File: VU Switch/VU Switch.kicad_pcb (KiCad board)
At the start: 2 copper layers, 99.1 x 59.7 mm, 2 parts

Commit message: Blank PCB
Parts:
- added M1: Mounting_pin, Mounting:M3, F.Cu at (104.8, 106.0)
- added M2: Mounting_pin, Mounting:M3, F.Cu at (197.5, 106.0)
- added M3: Mounting_pin, Mounting:M3, F.Cu at (197.5, 52.7)
- added M4: Mounting_pin, Mounting:M3, F.Cu at (104.8, 52.7)
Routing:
- added copper zone on B.Cu, net GND
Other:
- outline, holes or cut-outs redrawn

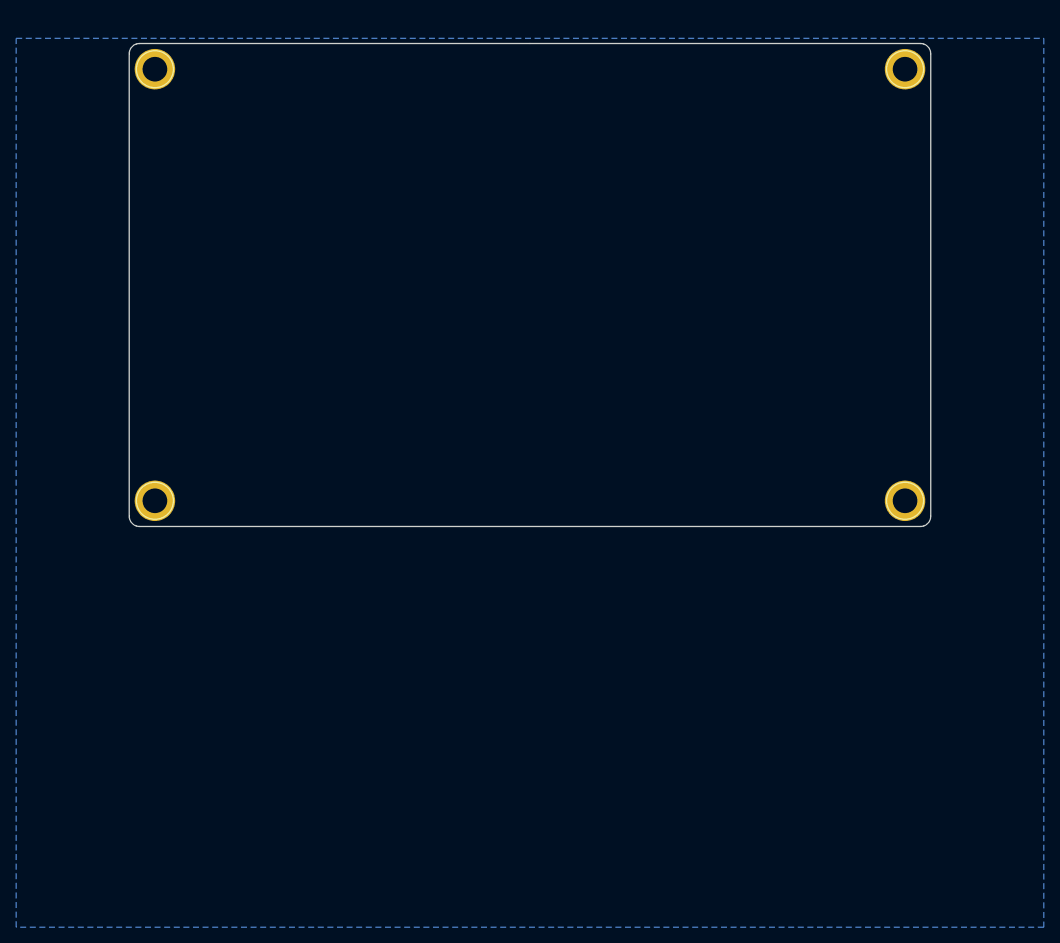
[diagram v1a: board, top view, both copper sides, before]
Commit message: Schematic done
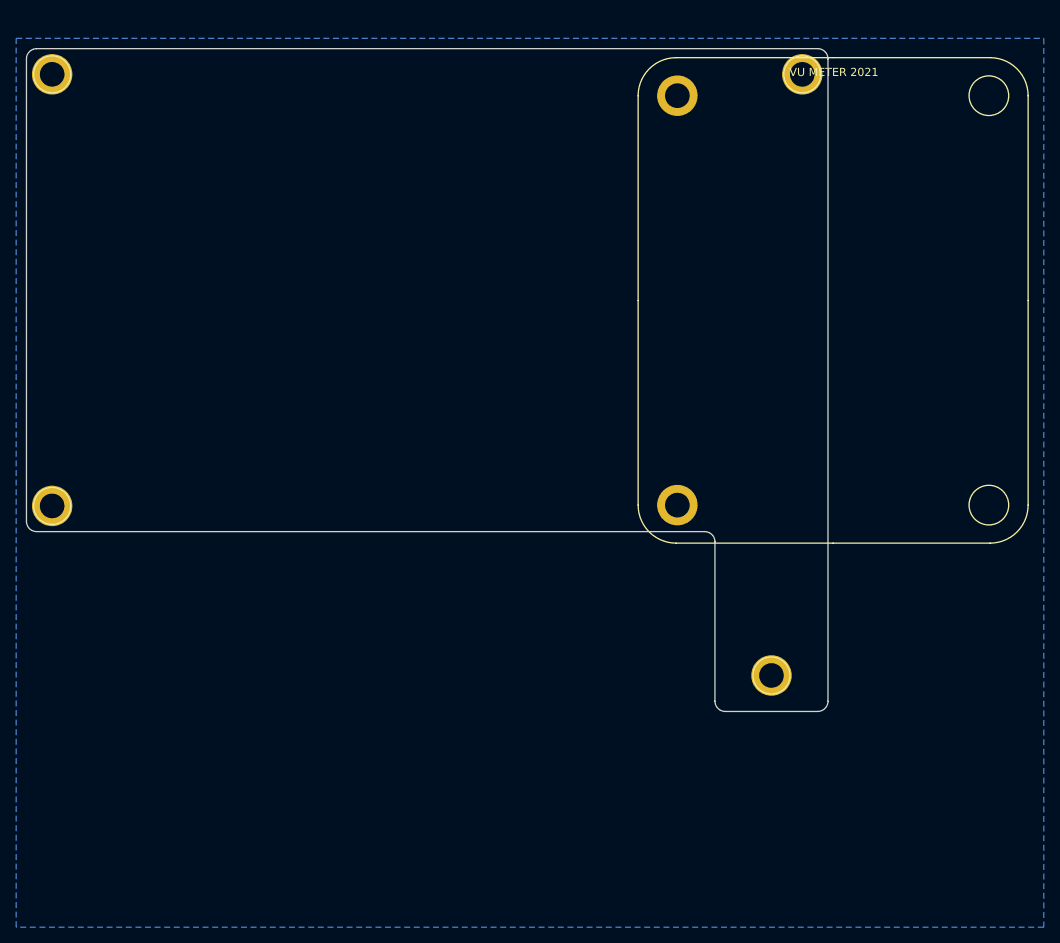
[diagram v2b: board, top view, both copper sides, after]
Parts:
- added A1: VU_Module, VU Switch:VU_Driver_Board_5.0, F.Cu at (188.6, 81.3)
- moved M2 27.2 mm to (181.0, 127.6)
- moved M3 12.7 mm to (184.8, 53.3)
- moved M1 12.7 mm to (92.1, 106.7)
- moved M4 12.7 mm to (92.1, 53.3)
- moved REF** 2.54 mm to (149.2, 149.2)
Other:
- board size 99.1 x 59.7 mm -> 99.1 x 81.9 mm

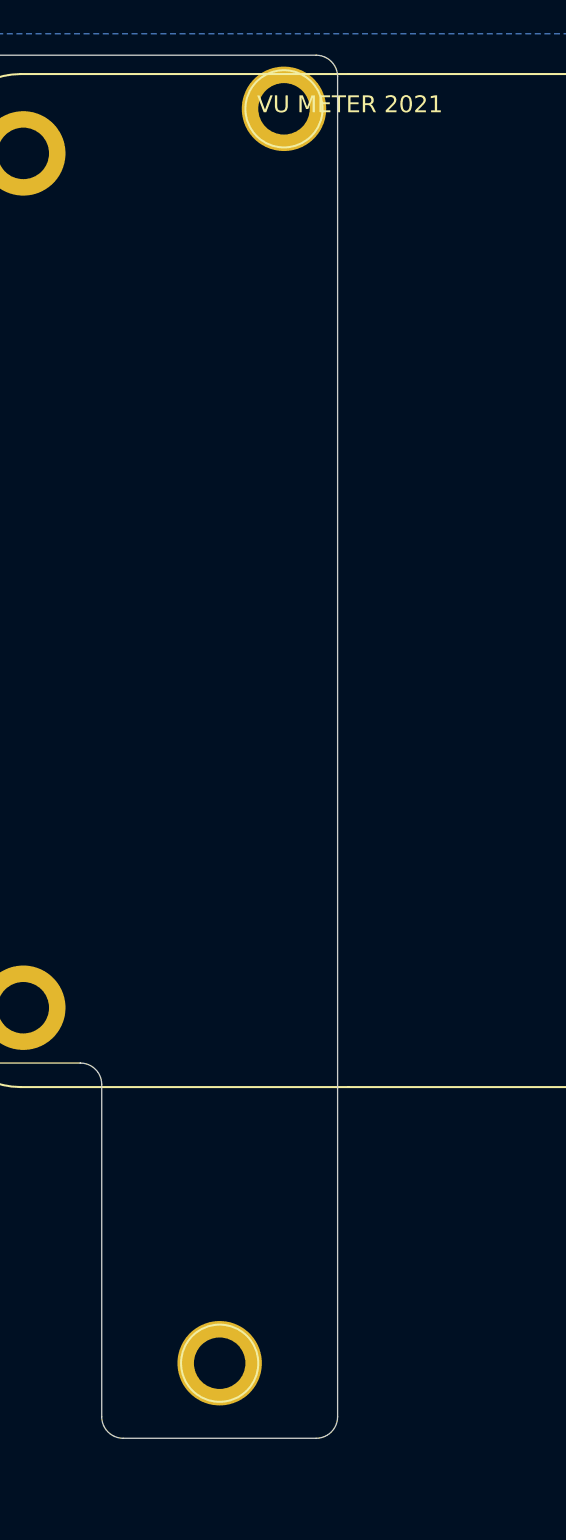
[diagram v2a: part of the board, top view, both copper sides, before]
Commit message: Assigned footprints
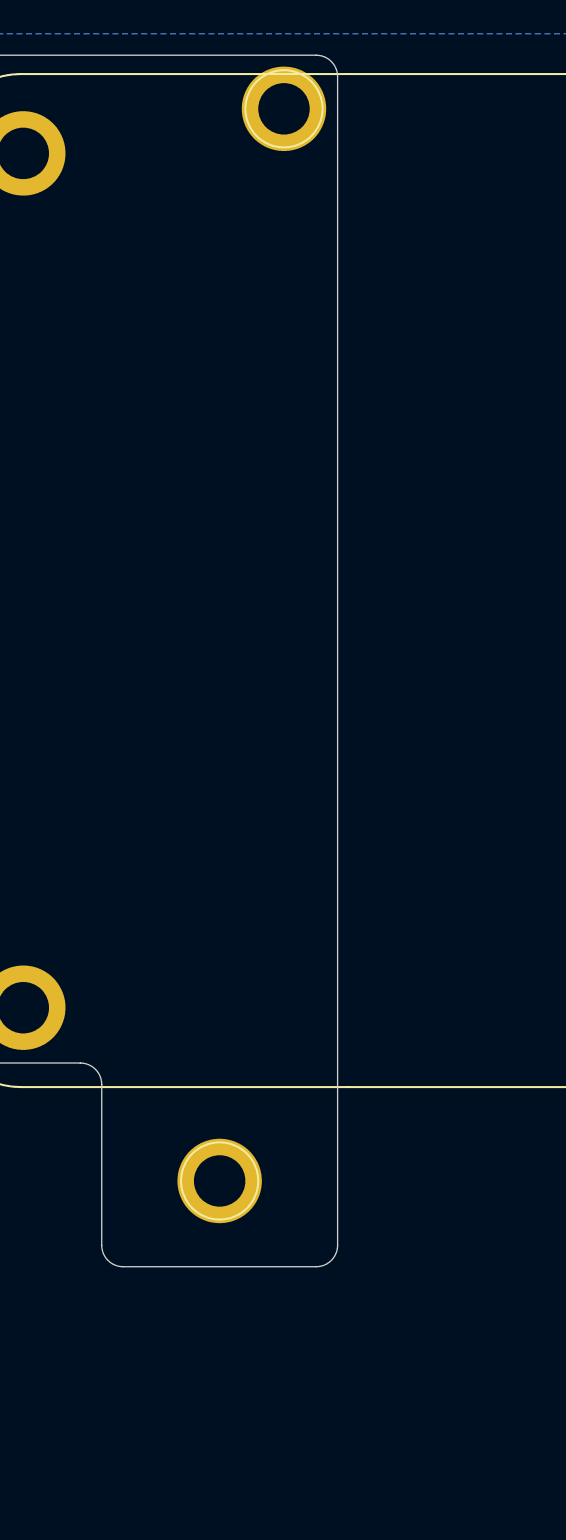
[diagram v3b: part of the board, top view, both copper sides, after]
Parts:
- moved M2 10.8 mm to (181.0, 116.8)
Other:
- board size 99.1 x 81.9 mm -> 99.1 x 71.8 mm
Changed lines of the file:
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@@
       (effects (font (size 1 1) (thickness 0.15)))
     )
-    (fp_text user "VU METER 2021" (at 0.1 -28.2) (layer F.SilkS)
+    (fp_text user "VU METER 2021" (at -12.7 -29.21) (layer Dwgs.User)
       (effects (font (size 1 1) (thickness 0.15)))
     )
@@
     (fp_arc (start 19.4 25.3) (end 19.4 30) (angle -90) (layer F.SilkS) (width 0.12))
     (fp_arc (start -19.4 -25.3) (end -19.4 -30) (angle -90) (layer F.SilkS) (width 0.12))
+    (fp_circle (center 19.25 25.3) (end 21.7 25.3) (layer F.SilkS) (width 0.12))
+    (fp_circle (center 19.25 -25.3) (end 21.7 -25.3) (layer F.SilkS) (width 0.12))
+    (fp_line (start -24.1 -25.3) (end -24.1 0) (layer F.SilkS) (width 0.12))
+    (fp_line (start 24.1 -25.3) (end 24.1 0) (layer F.SilkS) (width 0.12))
+    (fp_line (start 0 -30) (end -19.4 -30) (layer F.SilkS) (width 0.12))
+    (fp_line (start 0 -30) (end 19.4 -30) (layer F.SilkS) (width 0.12))
+    (fp_line (start -24.1 25.3) (end -24.1 0) (layer F.SilkS) (width 0.12))
+    (fp_line (start 24.1 25.3) (end 24.1 0) (layer F.SilkS) (width 0.12))
+    (fp_line (start 0 30) (end -19.4 30) (layer F.SilkS) (width 0.12))
     (fp_line (start 0 30) (end 19.4 30) (layer F.SilkS) (width 0.12))
-    (fp_line (start 0 30) (end -19.4 30) (layer F.SilkS) (width 0.12))
-    (fp_line (start 24.1 25.3) (end 24.1 0) (layer F.SilkS) (width 0.12))
-    (fp_line (start -24.1 25.3) (end -24.1 0) (layer F.SilkS) (width 0.12))
-    (fp_line (start 0 -30) (end 19.4 -30) (layer F.SilkS) (width 0.12))
-    (fp_line (start 0 -30) (end -19.4 -30) (layer F.SilkS) (width 0.12))
-    (fp_line (start 24.1 -25.3) (end 24.1 0) (layer F.SilkS) (width 0.12))
-    (fp_line (start -24.1 -25.3) (end -24.1 0) (layer F.SilkS) (width 0.12))
-    (fp_circle (center 19.25 -25.3) (end 21.7 -25.3) (layer F.SilkS) (width 0.12))
-    (fp_circle (center 19.25 25.3) (end 21.7 25.3) (layer F.SilkS) (width 0.12))
     (pad "" np_thru_hole circle (at -19.25 25.3 180) (size 5 5) (drill 3.048) (layers *.Cu *.Mask))
     (pad "" np_thru_hole circle (at -19.25 -25.3) (size 5 5) (drill 3.048) (layers *.Cu *.Mask))
@@
   )
   (module Mounting:M3 (layer F.Cu)
-    (at 180.975 127.635)
+    (at 180.975 116.84)
     (descr "module 1 pin (ou trou mecanique de percage)")
     (tags DEV)
@@
       (net 1 GND))
   )
-  (gr_line (start 175.26 132.08) (end 186.69 132.08) (layer Edge.Cuts) (width 0.05))
-  (gr_line (start 173.99 111.125) (end 173.99 130.81) (layer Edge.Cuts) (width 0.05))
+  (gr_line (start 175.26 121.92) (end 186.69 121.92) (layer Edge.Cuts) (width 0.05))
+  (gr_line (start 173.99 111.125) (end 173.99 120.65) (layer Edge.Cuts) (width 0.05))
   (gr_arc (start 172.72 111.125) (end 173.99 111.125) (angle -90) (layer Edge.Cuts) (width 0.05))
-  (gr_arc (start 175.26 130.81) (end 173.99 130.81) (angle -90) (layer Edge.Cuts) (width 0.05))
+  (gr_arc (start 175.26 120.65) (end 173.99 120.65) (angle -90) (layer Edge.Cuts) (width 0.05))
   (gr_arc (start 186.69 51.435) (end 187.96 51.435) (angle -90) (layer Edge.Cuts) (width 0.05))
-  (gr_arc (start 186.69 130.81) (end 186.69 132.08) (angle -90) (layer Edge.Cuts) (width 0.05))
+  (gr_arc (start 186.69 120.65) (end 186.69 121.92) (angle -90) (layer Edge.Cuts) (width 0.05))
   (gr_arc (start 90.17 108.585) (end 88.9 108.585) (angle -90) (layer Edge.Cuts) (width 0.05))
   (gr_arc (start 90.17 51.435) (end 90.17 50.165) (angle -90) (layer Edge.Cuts) (width 0.05))
   (gr_line (start 186.69 50.165) (end 138.43 50.165) (layer Edge.Cuts) (width 0.05))
-  (gr_line (start 187.96 130.81) (end 187.96 51.435) (layer Edge.Cuts) (width 0.05))
+  (gr_line (start 187.96 120.65) (end 187.96 51.435) (layer Edge.Cuts) (width 0.05))
   (gr_line (start 90.17 109.855) (end 172.72 109.855) (layer Edge.Cuts) (width 0.05))
   (gr_line (start 88.9 51.435) (end 88.9 108.585) (layer Edge.Cuts) (width 0.05))

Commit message: Layout done
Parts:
- added C1: 2200uF, Capacitor_THT:CP_Radial_D13.0mm_P5.00mm, F.Cu at (103.5, 83.8)
- added C2: 100uF, Capacitor_THT:CP_Radial_D6.3mm_P2.50mm, F.Cu at (102.9, 74.3)
- added C3: 100nF, Capacitor_THT:C_Disc_D4.7mm_W2.5mm_P5.00mm, F.Cu at (108.6, 75.6)
- added D1: 1n4007, Diode_THT:D_DO-41_SOD81_P10.16mm_Horizontal, F.Cu at (96.5, 89.5)
- added D2: 1n4001, Diode_THT:D_DO-41_SOD81_P10.16mm_Horizontal, F.Cu at (129.5, 97.8)
- added J1: DC_12V, TerminalBlock:TerminalBlock_bornier-2_P5.08mm, F.Cu at (93.3, 69.2)
- added J10: VU_12V, Connector_JST:JST_XH_B2B-XH-A_1x02_P2.50mm_Vertical, F.Cu at (160.7, 100.3)
- added J11: LED, Connector_JST:JST_XH_B2B-XH-A_1x02_P2.50mm_Vertical, F.Cu at (148.6, 91.4)
- added J12: VU_5V, Connector_JST:JST_XH_B2B-XH-A_1x02_P2.50mm_Vertical, F.Cu at (139.1, 91.4)
- added J13: VU_12V, Connector_JST:JST_XH_B2B-XH-A_1x02_P2.50mm_Vertical, F.Cu at (151.1, 100.3)
- added J2: VU_12V, Connector_JST:JST_XH_B2B-XH-A_1x02_P2.50mm_Vertical, F.Cu at (141.6, 100.3)
- added J3: SELECT, Connector_JST:JST_XH_B5B-XH-A_1x05_P2.50mm_Vertical, F.Cu at (129.4, 91.4)
- added J4: INPUT1, audio_jack:Tayda_3.5mm_stereo_TRS_jack_A-853, F.Cu at (157.5, 56.5)
- added J5: INPUT2, audio_jack:Tayda_3.5mm_stereo_TRS_jack_A-853, F.Cu at (144.8, 56.5)
- added J6: INPUT3, audio_jack:Tayda_3.5mm_stereo_TRS_jack_A-853, F.Cu at (132.1, 56.5)
- added J7: INPUT4, audio_jack:Tayda_3.5mm_stereo_TRS_jack_A-853, F.Cu at (119.4, 56.5)
- added J8: OUTPUT, audio_jack:Tayda_3.5mm_stereo_TRS_jack_A-853, F.Cu at (102.2, 56.5)
- added J9: VU_OUT, Connector_JST:JST_XH_B3B-XH-A_1x03_P2.50mm_Vertical, F.Cu at (160.7, 91.4)
- added K1: HK19F-DC, HK19F-DC:HK19F-DC, F.Cu at (161.3, 83.8)
- added K2: HK19F-DC, HK19F-DC:HK19F-DC, F.Cu at (148.6, 83.8)
- added K3: HK19F-DC, HK19F-DC:HK19F-DC, F.Cu at (135.9, 83.8)
- added K4: HK19F-DC, HK19F-DC:HK19F-DC, F.Cu at (123.2, 83.8)
- added R1: 1k, Resistor_THT:R_Axial_DIN0207_L6.3mm_D2.5mm_P10.16mm_Horizontal, F.Cu at (129.5, 101.6)
- added U1: LM7805_TO220, Package_TO_SOT_THT:TO-220-3_Vertical, F.Cu at (92.7, 87.0)
- moved M1 5.08 mm to (92.1, 101.6)
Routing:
- net +5V: track 0.00 -> 112.8 mm, vias 0 -> 2
- net +12V: track 0.00 -> 96.7 mm
- net OUT_R: track 0.00 -> 94.2 mm
- net OUT_L: track 0.00 -> 93.2 mm
- net SELECT_1: track 0.00 -> 35.9 mm, vias 0 -> 2
- net SELECT_2: track 0.00 -> 27.8 mm, vias 0 -> 2
- net Net-(J11-Pad1): track 0.00 -> 27.0 mm
- net SELECT_4: track 0.00 -> 13.2 mm
- net SELECT_3: track 0.00 -> 10.8 mm
- net Net-(D1-Pad2): track 0.00 -> 7.51 mm
- net Net-(J6-Pad2): track 0.00 -> 6.61 mm
- net Net-(J6-Pad5): track 0.00 -> 6.61 mm
- net Net-(J7-Pad5): track 0.00 -> 6.61 mm
- net Net-(J7-Pad2): track 0.00 -> 6.61 mm
- net Net-(J5-Pad5): track 0.00 -> 6.61 mm
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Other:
- outline, holes or cut-outs redrawn
- net class AUD added: clearance 0.2, trace_width 0.381, via_dia 0.8, via_drill 0.4
- net class PWR added: clearance 0.2, trace_width 0.381, via_dia 0.8, via_drill 0.4
- board text added: "12V"
- board text added: "1N 4001"
- board text added: "1N 4007"
- board text added: "GND"
- board text added: "LM7805"
- board text added: "VU Switch Revision A github.com/tebl"

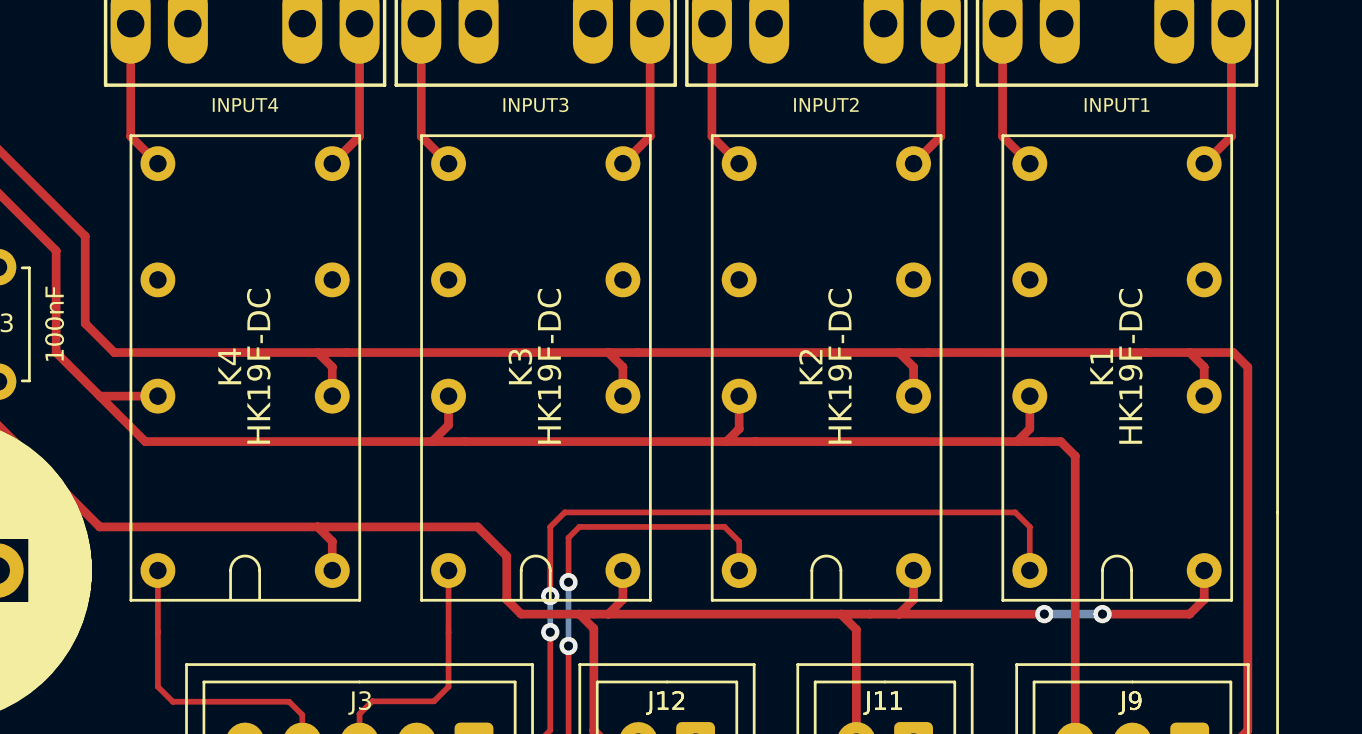
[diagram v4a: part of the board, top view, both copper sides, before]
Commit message: Changed HK19 relay footprint to larger pads
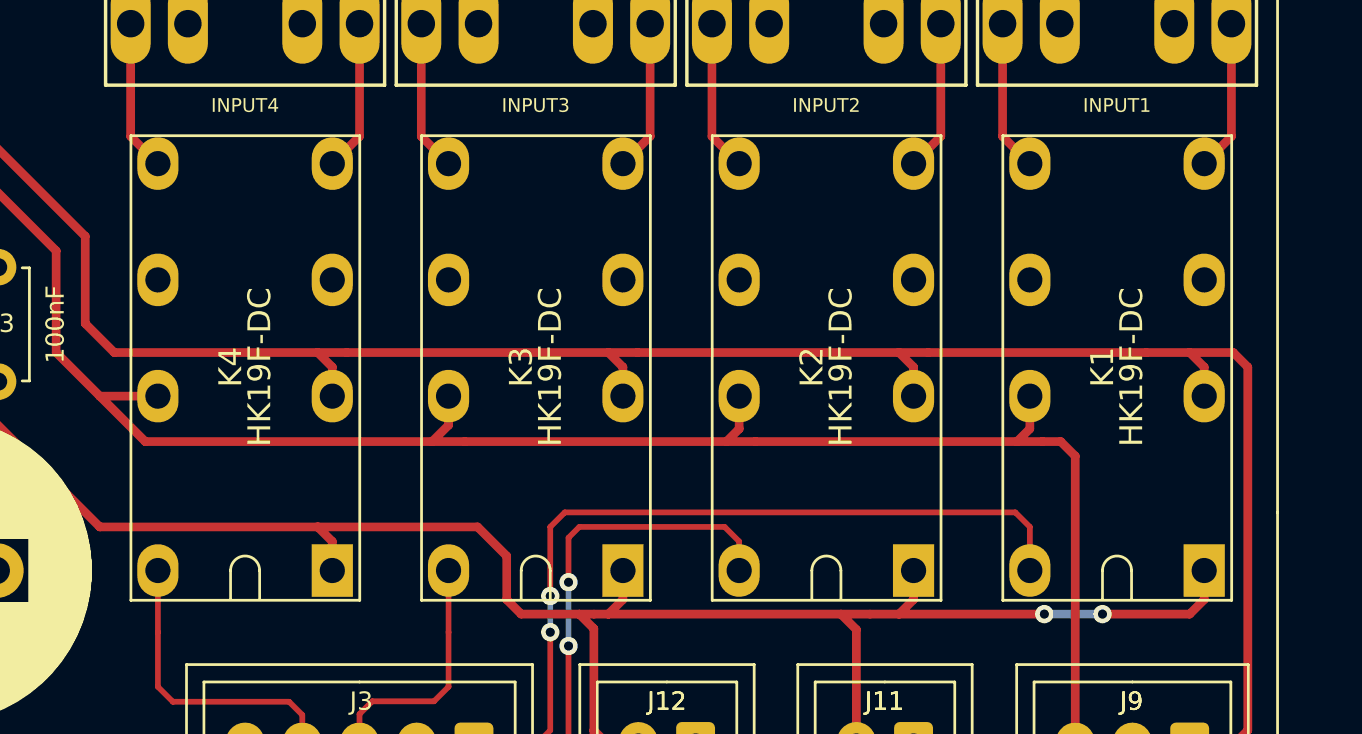
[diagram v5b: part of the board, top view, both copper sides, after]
